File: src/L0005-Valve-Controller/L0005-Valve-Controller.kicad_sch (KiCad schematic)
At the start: 44 parts, among them J1 Jumper_NO, J2 Jumper_NO, P1 3220-20-0200-00, P14 647676-3, P15 647676-3, P16 647676-2, P2 140-504-415-000, P9 647676-2, U1 LPC54113J256BD64QL, U2 LMS8117AMP-3.3_NOPB, U5 Optocoupler

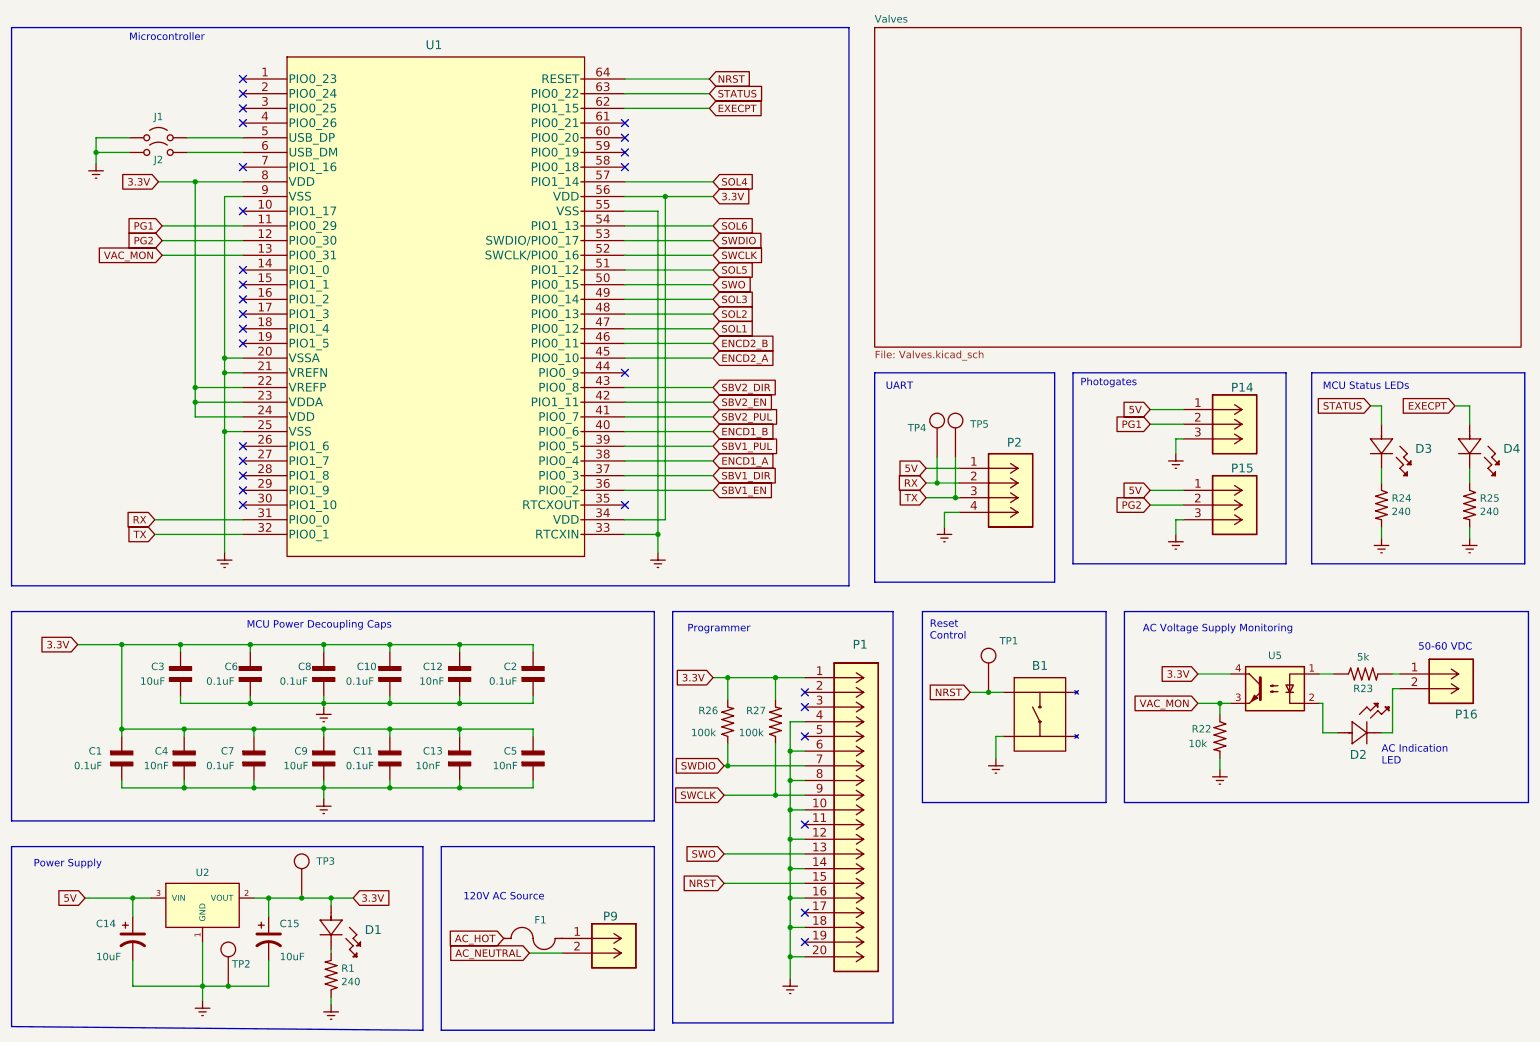
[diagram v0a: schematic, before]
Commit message: changed LED current limiters to 470 Ohm
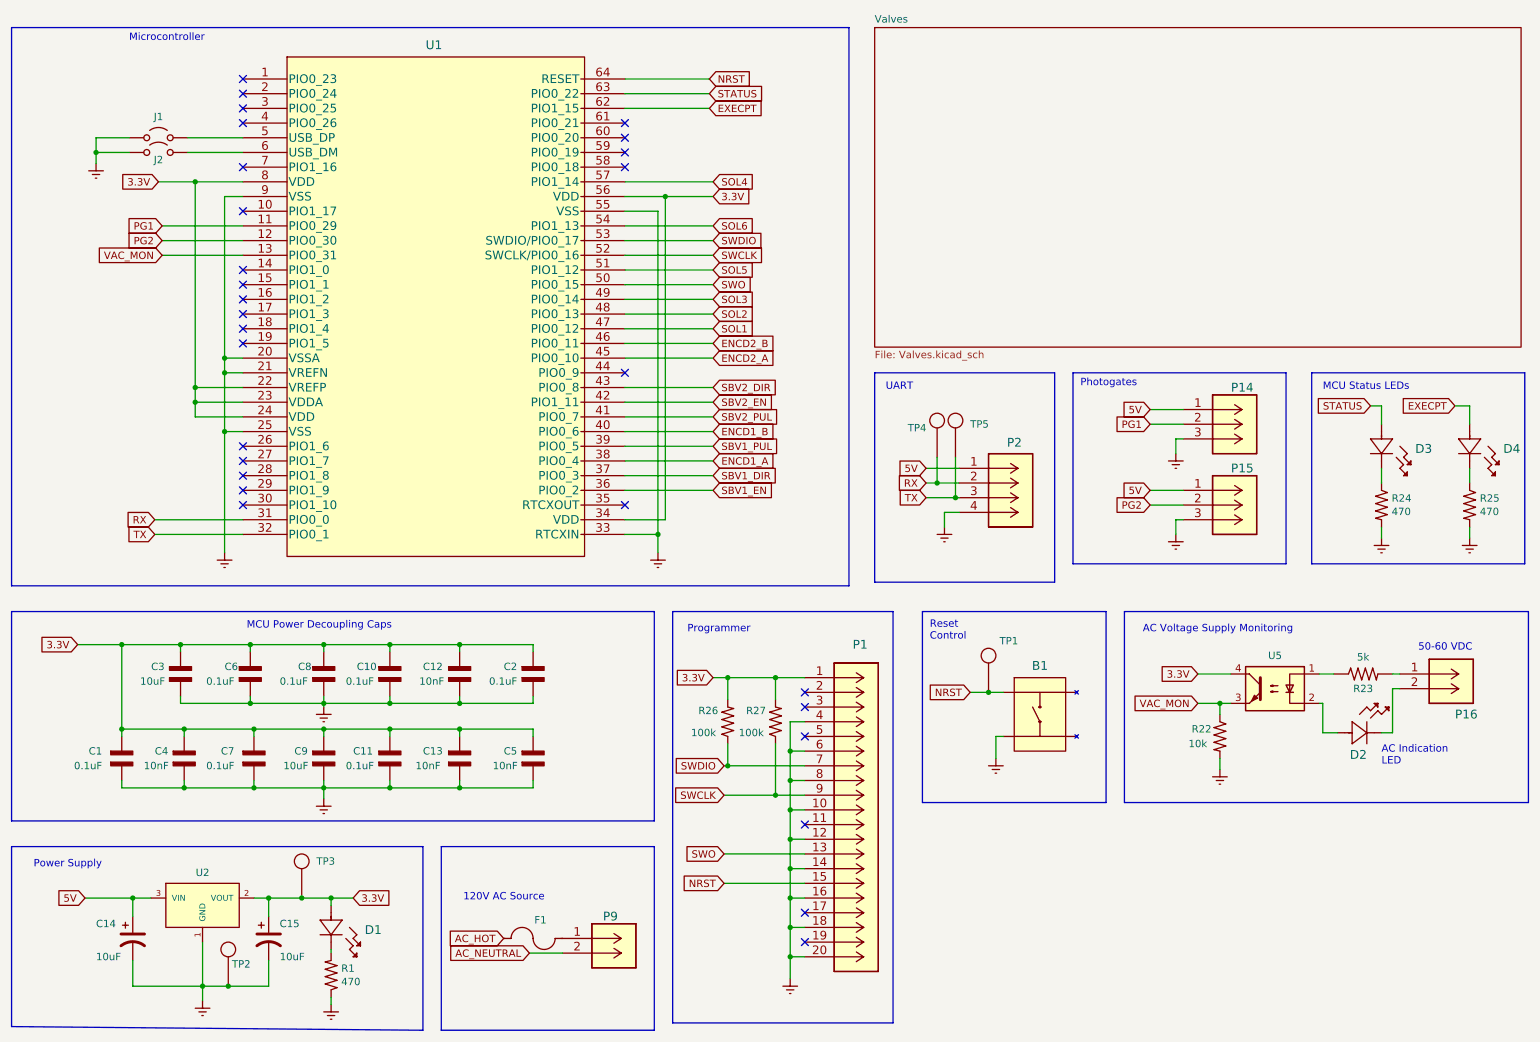
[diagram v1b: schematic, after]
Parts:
- R1, R24, R25: value 240 -> 470
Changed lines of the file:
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@@
       (effects (font (size 1.27 1.27)) (justify left))
     )
-    (property "Value" "240" (id 1) (at 76.6826 185.293 90)
+    (property "Value" "470" (id 1) (at 76.6826 185.293 90)
       (effects (font (size 1.27 1.27)) (justify left))
     )
@@
       (effects (font (size 1.27 1.27)) (justify left))
     )
-    (property "Value" "240" (id 1) (at 258.2926 104.013 90)
+    (property "Value" "470" (id 1) (at 258.2926 104.013 90)
       (effects (font (size 1.27 1.27)) (justify left))
     )
@@
       (effects (font (size 1.27 1.27)) (justify left))
     )
-    (property "Value" "240" (id 1) (at 273.5326 104.013 90)
+    (property "Value" "470" (id 1) (at 273.5326 104.013 90)
       (effects (font (size 1.27 1.27)) (justify left))
     )
@@
     )
     (path "/00000000-0000-0000-0000-000061fed053"
-      (reference "R1") (unit 1) (value "240") (footprint "L0005-Valve-Controller:RES_0603")
+      (reference "R1") (unit 1) (value "470") (footprint "L0005-Valve-Controller:RES_0603")
     )
     (path "/00000000-0000-0000-0000-0000624aa92c/00000000-0000-0000-0000-0000624b39e0"
@@
     )
     (path "/00000000-0000-0000-0000-00006201850d"
-      (reference "R24") (unit 1) (value "240") (footprint "L0005-Valve-Controller:RES_0603")
+      (reference "R24") (unit 1) (value "470") (footprint "L0005-Valve-Controller:RES_0603")
     )
     (path "/00000000-0000-0000-0000-00006207a00f"
-      (reference "R25") (unit 1) (value "240") (footprint "L0005-Valve-Controller:RES_0603")
+      (reference "R25") (unit 1) (value "470") (footprint "L0005-Valve-Controller:RES_0603")
     )
     (path "/05626d24-7f3e-4329-afec-c3037d7d39d9"

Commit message: rerouted PCB to include 5V logic MOSFETS
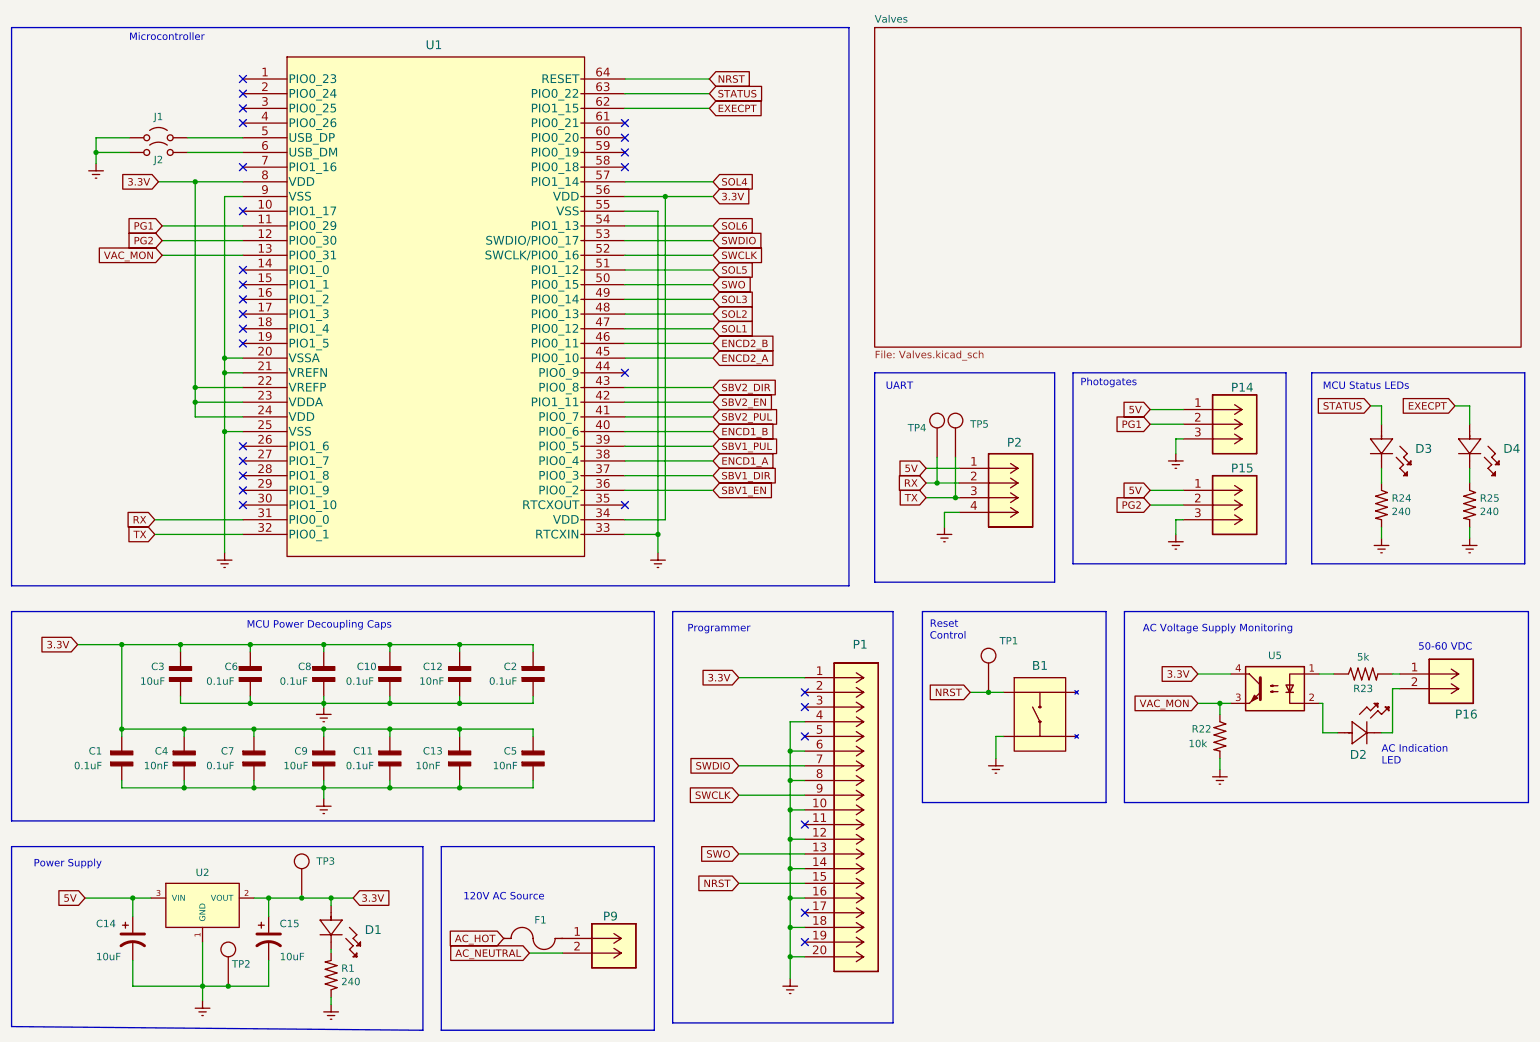
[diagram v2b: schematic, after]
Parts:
- removed R26, R27: 100k, symbol L0005-Valve-Controller:RES_0603
- C14, C15: footprint Engine-Controller:CWR11HH106KB -> L0005-Valve-Controller:CWR11HH106KB
- R1, R24, R25: value 470 -> 240

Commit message: produced gerbers files
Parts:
- C14, C15: footprint L0005-Valve-Controller:CWR11HH106KB -> L0005-Valve-Controller:T491A106K010AT
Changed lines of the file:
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@@
       (effects (font (size 1.27 1.27)) (justify left))
     )
-    (property "Footprint" "L0005-Valve-Controller:CWR11HH106KB" (id 2) (at 40.64 177.8 0)
+    (property "Footprint" "L0005-Valve-Controller:T491A106K010AT" (id 2) (at 40.64 177.8 0)
       (effects (font (size 1.27 1.27)) hide)
     )
@@
       (effects (font (size 1.27 1.27)) (justify left))
     )
-    (property "Footprint" "L0005-Valve-Controller:CWR11HH106KB" (id 2) (at 64.135 177.8 0)
+    (property "Footprint" "L0005-Valve-Controller:T491A106K010AT" (id 2) (at 64.135 177.8 0)
       (effects (font (size 1.27 1.27)) hide)
     )
@@
     )
     (path "/00000000-0000-0000-0000-000061fb83f5"
-      (reference "C14") (unit 1) (value "10uF") (footprint "L0005-Valve-Controller:CWR11HH106KB")
+      (reference "C14") (unit 1) (value "10uF") (footprint "L0005-Valve-Controller:T491A106K010AT")
     )
     (path "/00000000-0000-0000-0000-000061fc4d2a"
-      (reference "C15") (unit 1) (value "10uF") (footprint "L0005-Valve-Controller:CWR11HH106KB")
+      (reference "C15") (unit 1) (value "10uF") (footprint "L0005-Valve-Controller:T491A106K010AT")
     )
     (path "/00000000-0000-0000-0000-0000624aa92c/00000000-0000-0000-0000-0000624b39fe"
